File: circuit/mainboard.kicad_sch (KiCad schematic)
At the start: 18 parts, among them J1 RJ45, J2 RJ45, J3 Conn_01x04_Pin, J4 Conn_01x04_Pin, J5 Conn_01x07_Pin, J6 Conn_01x07_Pin, U2 LM7805_TO220

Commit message: schematic first pass
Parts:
- added BT1: 5xAA, symbol Device:Battery
- added C1: 0.1, symbol Device:C
- added C2: 0.22, symbol Device:C_Polarized_US
- added D4: ERROR_LED, symbol Device:LED
- added J10: BEAM_EMIT_RIGHT, symbol Connector:Conn_01x02_Pin
- added J11: UNUSED_PINS, symbol Connector:Conn_01x09_Pin
- added J7: BEAM_SENSE_LEFT, symbol Connector:Conn_01x03_Pin
- added J8: BEAM_SENSE_RIGHT, symbol Connector:Conn_01x03_Pin
- added J9: BEAM_EMIT_LEFT, symbol Connector:Conn_01x02_Pin
- added R7: 220, symbol Device:R
- added SW1: POWER, symbol Switch:SW_SPDT
- J1: value RJ45 -> MOTOR_CONN
- J2: value RJ45 -> CTRLR_CONN
- J3: value Conn_01x04_Pin -> DISP_LEFT
- J4: value Conn_01x04_Pin -> DISP_RIGHT
- J6: value Conn_01x07_Pin -> LED_Conn
- U1: value ~ -> OLED_128x64
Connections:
- net +3V3: now also J11.2 (Pin_2)
- net 5V: now also A2.39 (VSYS), U2.3 (VO), C1.1, J10.1 (Pin_1), J11.1 (Pin_1), J7.1 (Pin_1), J8.1 (Pin_1), J9.1 (Pin_1)
- net GND: now also U2.2 (GND), BT1.2 (-), C1.2, C2.2, D4.1 (K), J10.2 (Pin_2), J11.9 (Pin_9), J7.3 (Pin_3), J8.3 (Pin_3), J9.2 (Pin_2)
- net at A2.20 (GPIO15): now also R7.2
- net GPIO16: now reaches A2.21 (GPIO16)
- net GPIO16: now also J11.3 (Pin_3)
- net GPIO17: now reaches A2.22 (GPIO17)
- net GPIO17: now also J11.4 (Pin_4)
- net GPIO18: now reaches A2.24 (GPIO18)
- net GPIO18: now also J11.5 (Pin_5)
- net GPIO19: now reaches A2.25 (GPIO19)
- net GPIO19: now also J11.6 (Pin_6)
- net GPIO20: now reaches A2.26 (GPIO20)
- net GPIO20: now also J11.7 (Pin_7)
- net LBEAM_SIG: now reaches A2.31 (GPIO26_ADC0)
- net LBEAM_SIG: now also J7.2 (Pin_2)
- net RBEAM_SIG: now reaches A2.32 (GPIO27_ADC1)
- net RBEAM_SIG: now also J8.2 (Pin_2)
- net GPIO28_ADC2: now reaches A2.34 (GPIO28_ADC2)
- net GPIO28_ADC2: now also J11.8 (Pin_8)
- net VBAT: now reaches U2.1 (VI)
- net VBAT: now also C2.1, SW1.3 (C)
- new net: BT1.1 (+), SW1.2 (B)
- new net: D4.2 (A), R7.1
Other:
- moved on the sheet: J1, J2, J3, J4, U2

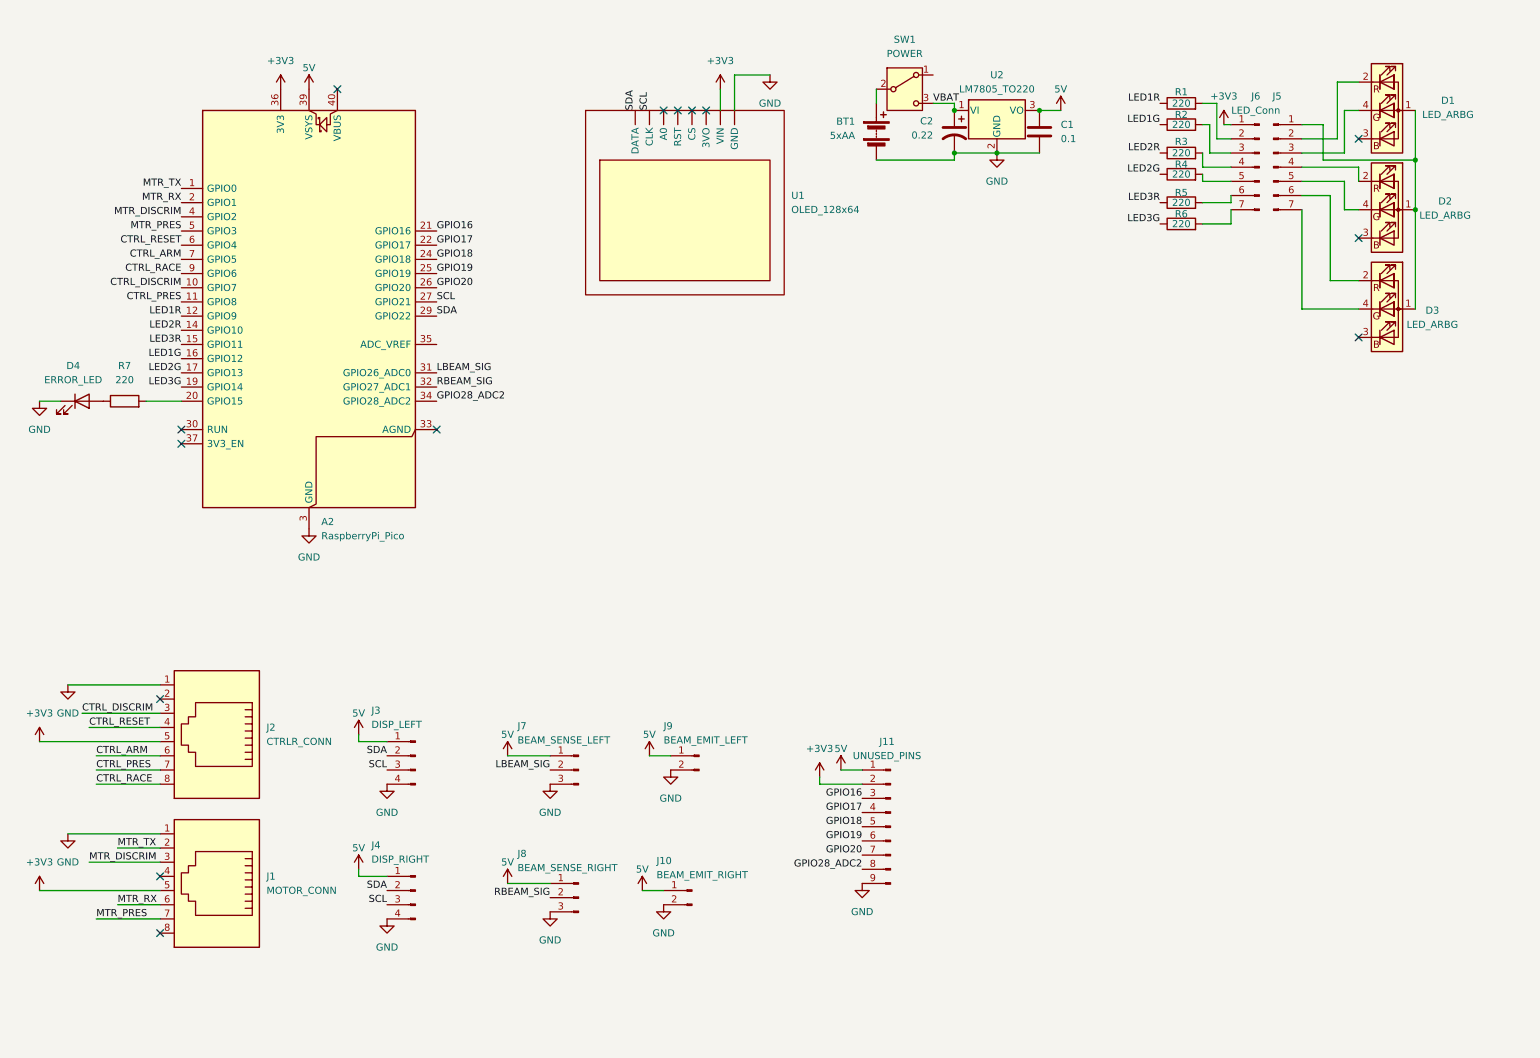
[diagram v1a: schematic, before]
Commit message: add LEDs to controller
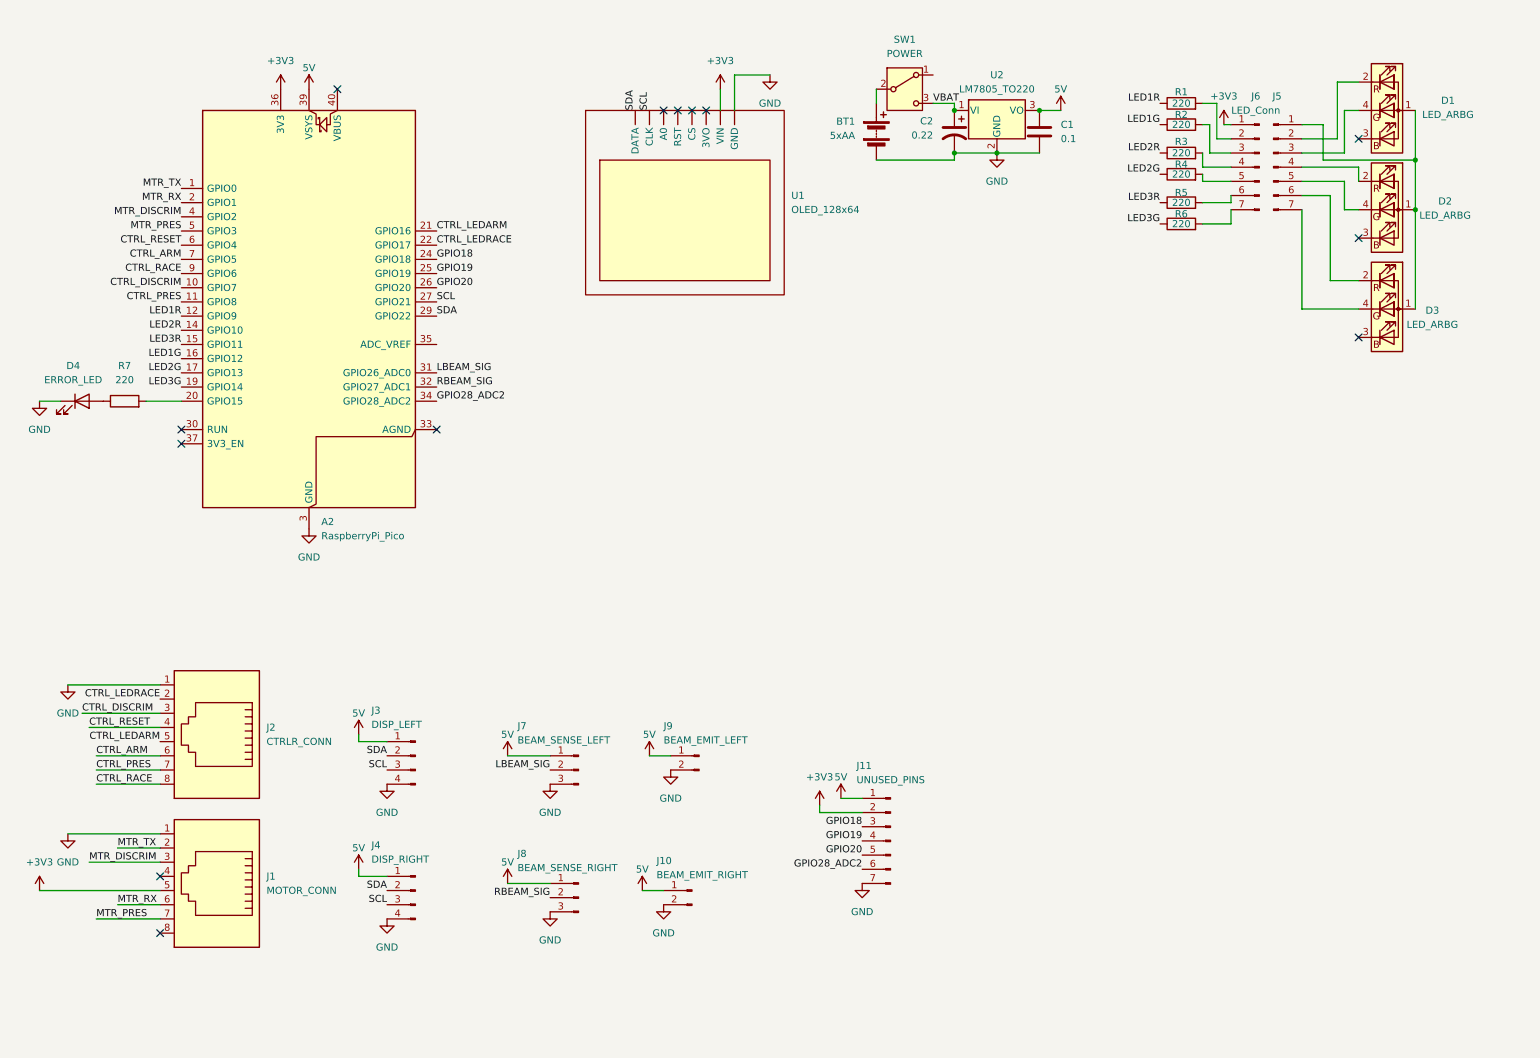
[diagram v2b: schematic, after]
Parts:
- removed J11: UNUSED_PINS, symbol Connector:Conn_01x09_Pin
- added J11: UNUSED_PINS, symbol Connector:Conn_01x07_Pin
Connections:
- net GPIO17 is gone; now on net CTRL_LEDRACE: A2.22 (GPIO17)
- net +3V3: now also J11.2 (Pin_2); no longer J2.5
- net 5V: now also J11.1 (Pin_1)
- net GND: now also J11.7 (Pin_7)
- net GPIO18: now also J11.3 (Pin_3)
- net GPIO19: now also J11.4 (Pin_4)
- net GPIO20: now also J11.5 (Pin_5)
- net GPIO28_ADC2: now also J11.6 (Pin_6)
- net CTRL_LEDRACE: now reaches J2.2
- net GPIO16 renamed CTRL_LEDARM
- net CTRL_LEDARM: now also J2.5
- no-connect marks 14 -> 13

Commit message: add footprints and organize sheet
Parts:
- A2: footprint Module_RaspberryPi_Pico:RaspberryPi_Pico_Common -> Module:RaspberryPi_Pico_Common_THT
- BT1, J10, J9: footprint (none) -> Connector_PinHeader_2.54mm:PinHeader_1x02_P2.54mm_Horizontal
- C1: footprint (none) -> Capacitor_THT:C_Disc_D5.0mm_W2.5mm_P5.00mm
- C2: footprint (none) -> Capacitor_THT:CP_Radial_D8.0mm_P3.50mm
- D1, D2, D3: footprint (none) -> LED_THT:LED_D5.0mm-4_RGB
- D4: footprint (none) -> LED_THT:LED_D5.0mm
- J1, J2: footprint (none) -> SparkFun_Connector:RJ45_Breakout_2.54mm
- J11: footprint (none) -> Connector_PinHeader_2.54mm:PinHeader_1x07_P2.54mm_Vertical; now not fitted
- J3, J4: footprint (none) -> Connector_PinHeader_2.54mm:PinHeader_1x04_P2.54mm_Horizontal
- J5, J6: footprint (none) -> Connector_PinHeader_2.54mm:PinHeader_1x07_P2.54mm_Vertical
- J7, J8: footprint (none) -> Connector_PinHeader_2.54mm:PinHeader_1x03_P2.54mm_Horizontal
- R1, R2, R3, R4, R5, R6, R7: footprint (none) -> Resistor_THT:R_Axial_DIN0207_L6.3mm_D2.5mm_P7.62mm_Horizontal
- SW1: footprint (none) -> Connector_PinSocket_2.54mm:PinSocket_1x03_P2.54mm_Vertical
- U1: footprint (none) -> Display:Adafruit_SSD1306_No_Mounting_Holes
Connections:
- net ERROR_LED: now reaches A2.20 (GPIO15), R7.2
- no-connect marks 13 -> 15
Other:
- note added: "Connections"
- note added: "Display"
- note added: "Microcontroller"
- note added: "Power circuitry"
- note added: "Starting LED passives"
- note added: "Starting LEDs"
- moved on the sheet: BT1, C1, C2, J1, J10, J2, J3, J4, J7, J8, J9, SW1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

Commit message: initial pcb layout
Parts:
- added H1, H2, H3, H4: MountingHole, MountingHole:MountingHole_3mm, symbol Mechanical:MountingHole
- C2: footprint Capacitor_THT:CP_Radial_D8.0mm_P3.50mm -> Capacitor_THT:CP_Radial_D4.0mm_P2.00mm
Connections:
- net +3V3: now also U1.7 (VIN); no longer U1. (VIN)
- net GND: now also U1.8 (GND); no longer U1. (VIN)
- net SCL: now also U1.2 (CLK); no longer U1. (VIN)
- net SDA: now also U1.1 (DATA); no longer U1. (VIN)
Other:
- note added: "Mounting holes"

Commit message: route PCB
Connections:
- net PRESWITCH: now reaches BT1.1 (+), SW1.2 (B)
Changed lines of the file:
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@@
+		)
+	)
+	(label "PRESWITCH"
+		(at 163.83 29.21 180)
+		(effects
+			(font
+				(size 1.27 1.27)
+			)
+			(justify right bottom)
 		)
 	)

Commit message: This is the board that was produced as rev1
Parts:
- added D5: 1N4001, Diode_THT:D_DO-41_SOD81_P10.16mm_Horizontal, symbol Device:D
- added JP1, JP2, JP3, JP4: ~, Jumper:SolderJumper-2_P1.3mm_Open_TrianglePad1.0x1.5mm, symbol Jumper:Jumper_2_Small_Open
- C2: footprint Capacitor_THT:CP_Radial_D4.0mm_P2.00mm -> Capacitor_THT:CP_Radial_D5.0mm_P2.00mm
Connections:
- net +3V3: now also JP2.2 (B)
- net 5V: now also D5.2 (A); no longer A2.39 (VSYS)
- net GND: now also JP1.2 (B)
- net SCL: now also JP3.2 (B)
- net SDA: now also JP4.2 (B)
- net at U1.3 (A0): now also JP1.1 (A)
- net at U1.4 (RST): now also JP2.1 (A)
- net at U1.5 (CS): now also JP3.1 (A)
- net at U1.6 (3VO): now also JP4.1 (A)
- new net VSYS: A2.39 (VSYS), D5.1 (K)
- no-connect marks 15 -> 11
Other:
- note added: "Bridge jumpers for generic OLED"
